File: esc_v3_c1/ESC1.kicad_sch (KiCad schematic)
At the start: 39 parts, among them J1 Power, J2 Inputs, J3 Output, Q1 IRF4905, Q10 S8050, Q11 S8050, Q12 S8050, Q2 IRF4905, Q3 IRF4905, Q4 S8050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

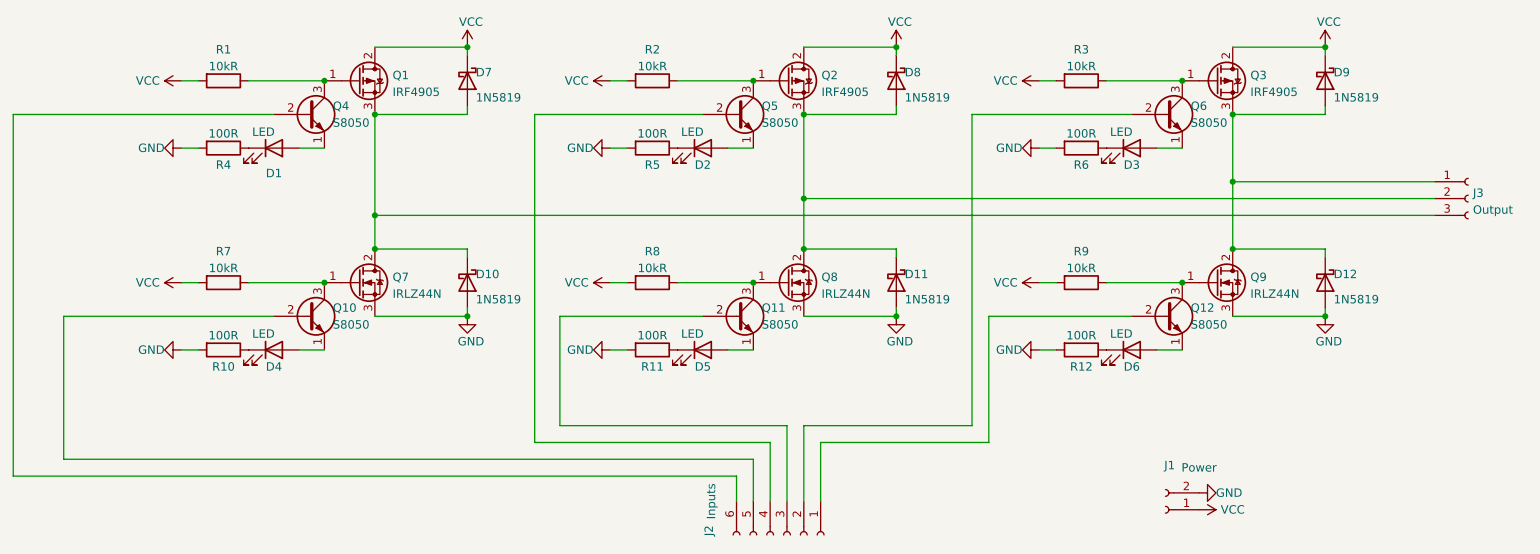
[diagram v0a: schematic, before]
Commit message: populate initial board layout
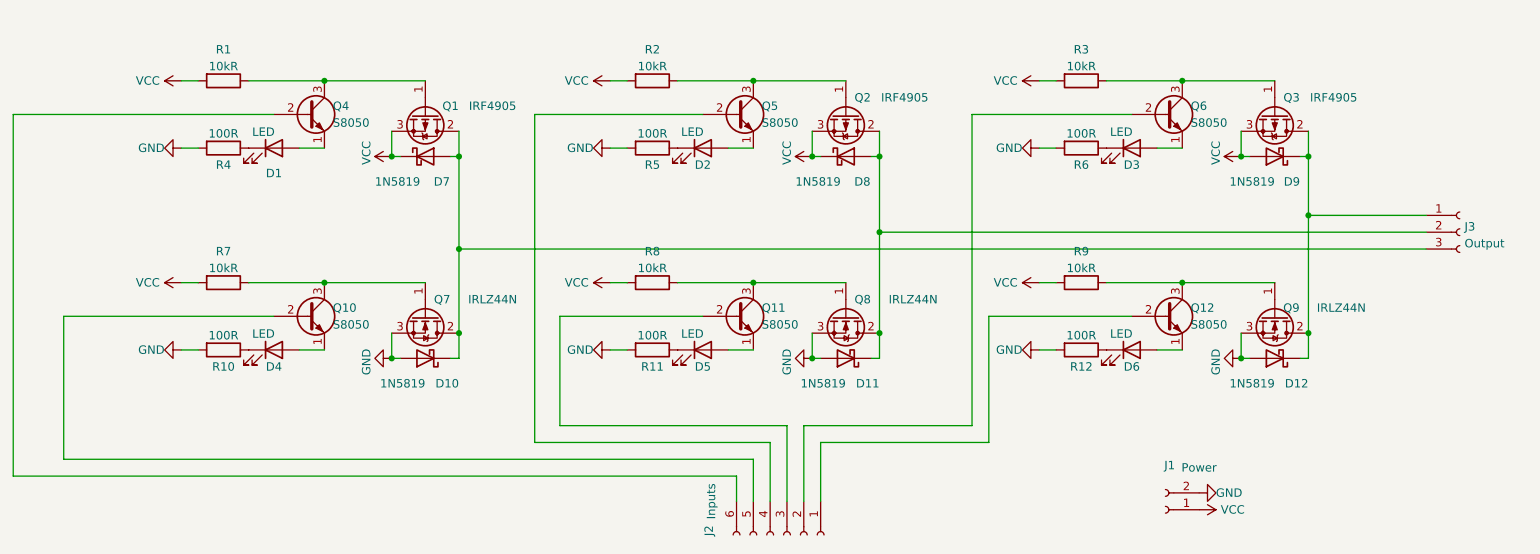
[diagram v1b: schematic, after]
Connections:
- net VCC: now also D9.2 (A), Q1.3 (S), Q2.3 (S), Q3.3 (S); no longer D9.1 (K), Q1.2 (D), Q2.2 (D), Q3.2 (D)
- net at D12.1 (K), J3.1 (Pin_1), Q9.2 (D): now also D9.1 (K), Q3.2 (D); no longer D9.2 (A), Q3.3 (S)
- net at D11.1 (K), D8.2 (A), J3.2 (Pin_2)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: now also Q2.2 (D); no longer Q2.3 (S)
- net at D10.1 (K), D7.2 (A), J3.3 (Pin_3)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: now also Q1.2 (D); no longer Q1.3 (S)
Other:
- moved on the sheet: D10, D11, D12, D7, D8, D9, J3, Q1, Q2, Q3, Q7, Q8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

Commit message: add plot files
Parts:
- J1: footprint Connector_JST:JST_XH_B2B-XH-AM_1x02_P2.50mm_Vertical -> Connector_JST:JST_XH_B2B-XH-A_1x02_P2.50mm_Vertical
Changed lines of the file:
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@@
     (property "Reference" "J1" (id 0) (at 220.345 121.573 0))
     (property "Value" "Power" (id 1) (at 224.79 121.92 0))
-    (property "Footprint" "Connector_JST:JST_XH_B2B-XH-AM_1x02_P2.50mm_Vertical" (id 2) (at 219.71 128.27 0)
+    (property "Footprint" "Connector_JST:JST_XH_B2B-XH-A_1x02_P2.50mm_Vertical" (id 2) (at 219.71 128.27 0)
       (effects (font (size 1.27 1.27)) hide)
     )
@@
     )
     (path "/d60029d3-771b-4d28-80d6-7eaf19bfd272"
-      (reference "J1") (unit 1) (value "Power") (footprint "Connector_JST:JST_XH_B2B-XH-AM_1x02_P2.50mm_Vertical")
+      (reference "J1") (unit 1) (value "Power") (footprint "Connector_JST:JST_XH_B2B-XH-A_1x02_P2.50mm_Vertical")
     )
     (path "/7d162526-a1b6-42b8-a404-3d5f0c26ea90"
